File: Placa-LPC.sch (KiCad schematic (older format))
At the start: 23 parts, among them K1 CONN_3, K2 CONN_3, K3 CONN_3, K4 CONN_3, P10 CONN_6, P11 CONN_6, P6 CONN_4X2, P7 CONN_8, P8 CONN_6, P9 CONN_6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

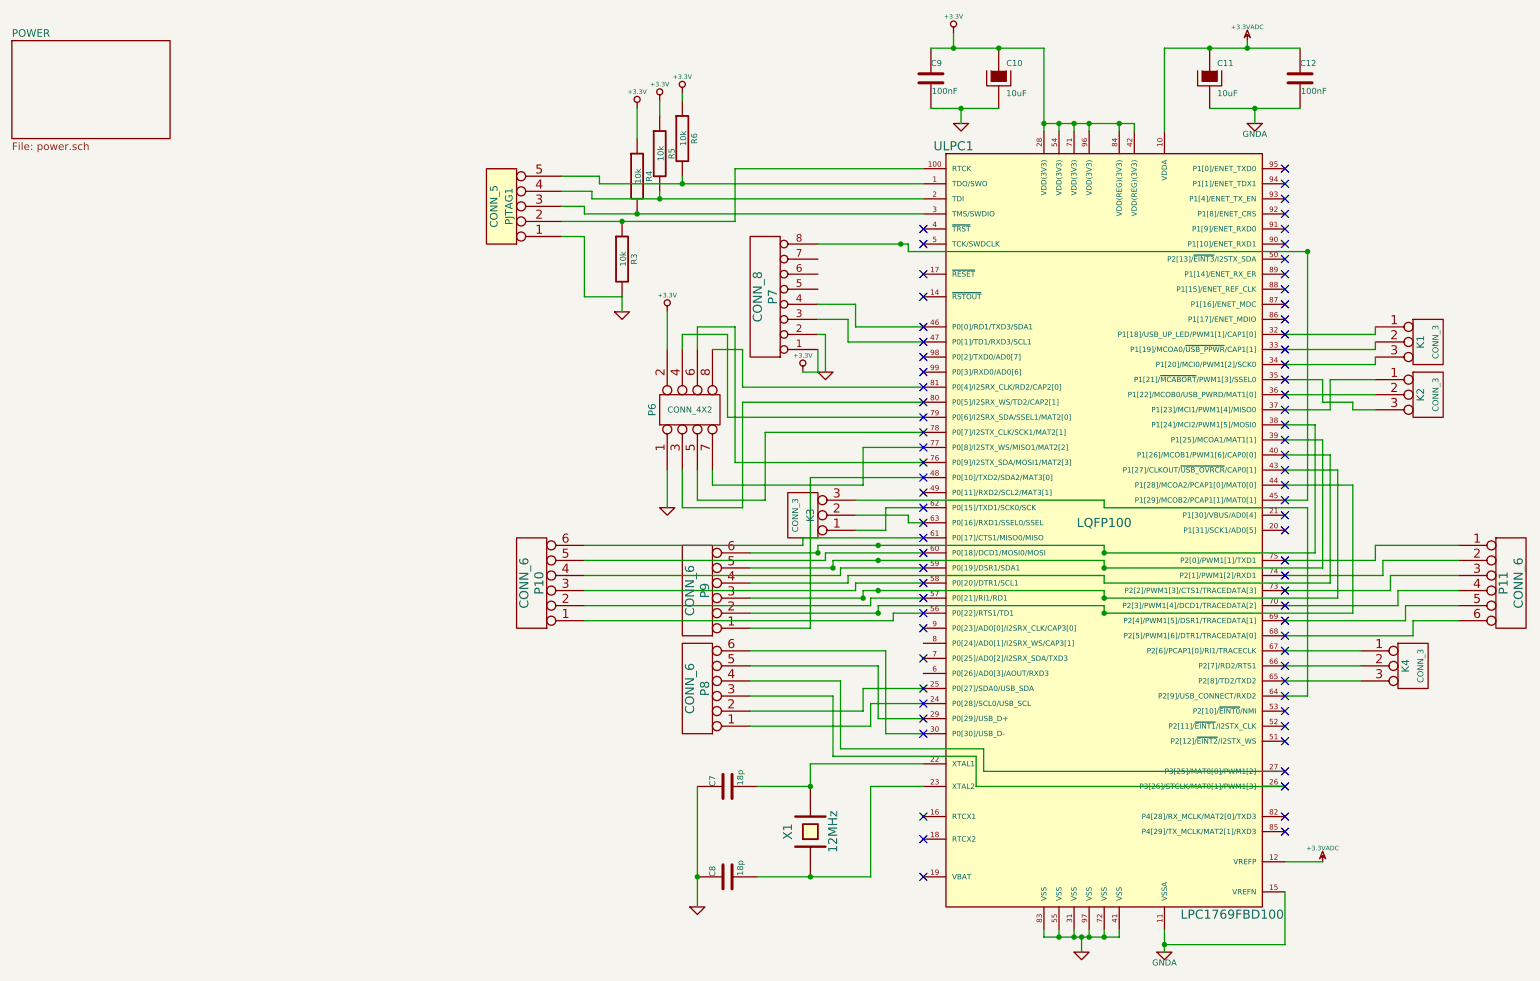
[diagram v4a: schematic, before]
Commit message: Agregado de...
Pines programacion jtag e isp
Resistencias pull-up puerto cero de entrada.
ADC para bateria y reset
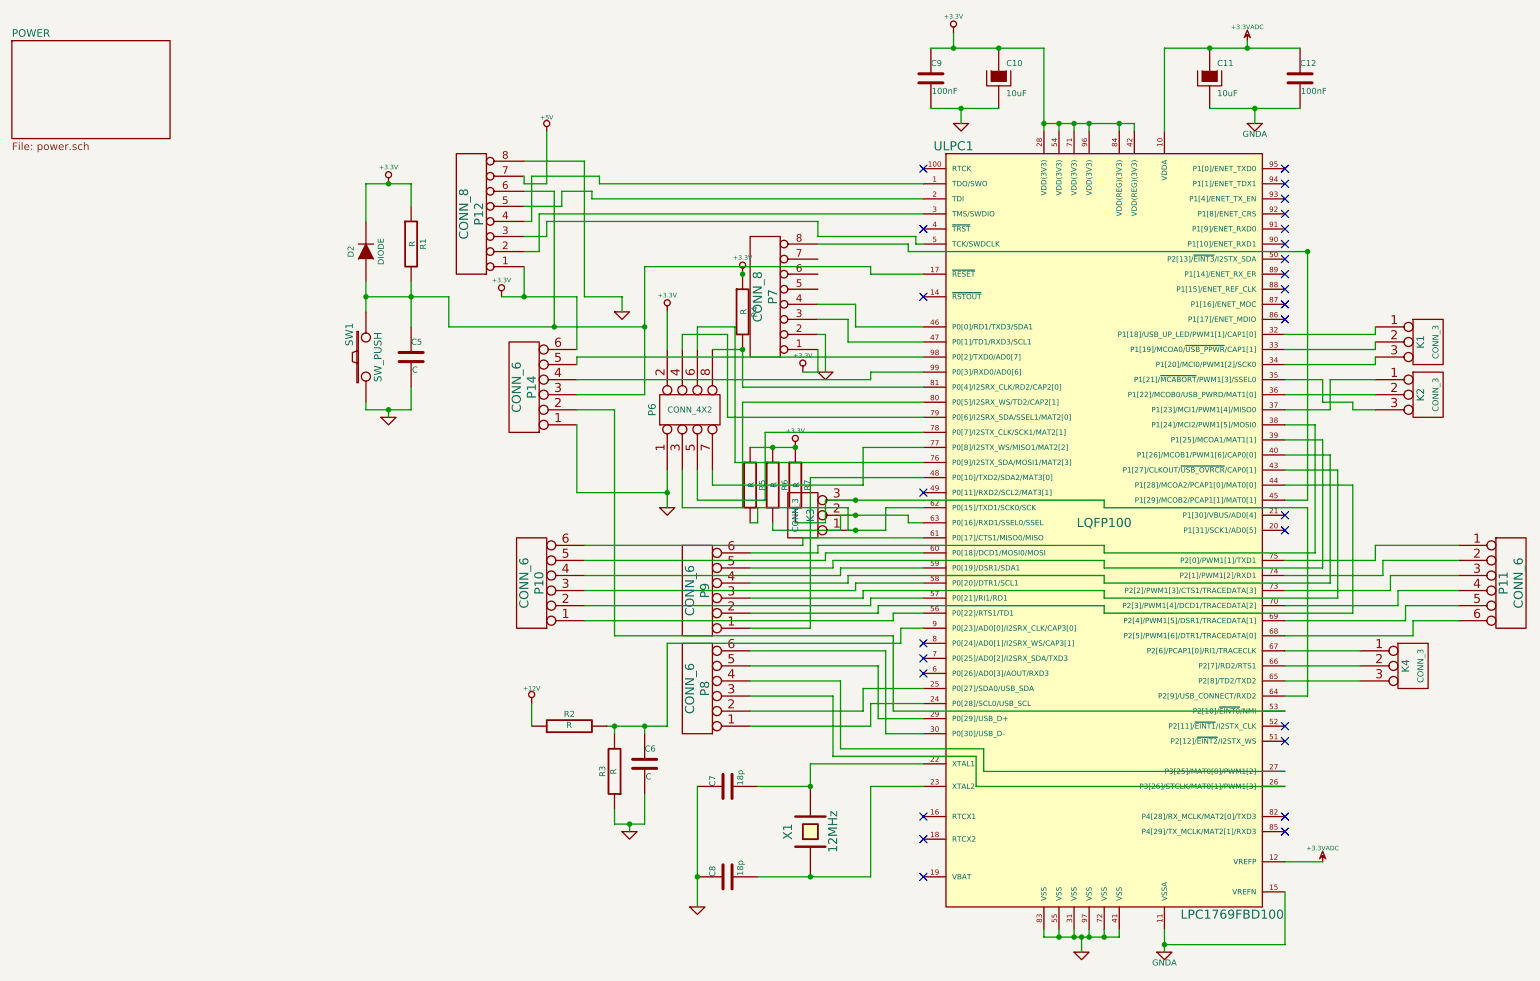
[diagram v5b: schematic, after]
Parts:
- removed PJTAG1: CONN_5, symbol CONN_5
- added C5, C6: C, ~, symbol C
- added D2: DIODE, ~, symbol DIODE
- added P12: CONN_8, symbol CONN_8
- added P14: CONN_6, symbol CONN_6
- added R1, R2, R7: R, ~, symbol R
- added SW1: SW_PUSH, ~, symbol SW_PUSH
- R3, R4, R5, R6: value 10k -> R
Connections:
- net +3.3V: now also D2.2 (K), P12.1 (P1), P14.6, R1.1, R7.1
- net GND: now also R3.1, C5.2, C6.2, P12.8 (P8), P14.1, SW1.1; no longer R3.2
- net at ULPC1.1 (TDO/SWO): now also P12.4 (P4); no longer R6.2
- net at ULPC1.100 (RTCK): no longer R3.1
- net at ULPC1.17 (~RESET~): now also C5.1, D2.1 (A), P12.6 (P6), P14.3, R1.2, SW1.2
- net at ULPC1.2 (TDI): now also P12.5 (P5); no longer R5.2
- net at ULPC1.3 (TMS/SWDIO): now also P12.2 (P2); no longer R4.2
- net at ULPC1.5 (TCK/SWDCLK): now also P12.3 (P3)
- net at ULPC1.53 (P2[10]/~EINT0~/NMI): now also P14.2
- net at K3.1 (P1), ULPC1.62 (P0[15]/TXD1/SCK0/SCK): now also R5.2
- net at K3.2 (PM), ULPC1.63 (P0[16]/RXD1/SSEL0/SSEL): now also R6.2
- net at K3.3 (P3), ULPC1.64 (P2[9]/USB_CONNECT/RXD2): now also R7.2
- net at P6.8, ULPC1.81 (P0[4]/I2SRX_CLK/RD2/CAP2[0]): now also R4.2
- net at ULPC1.9 (P0[23]/AD0[0]/I2SRX_CLK/CAP3[0]): now also R3.2, C6.1, R2.2
- net at ULPC1.98 (P0[2]/TXD0/AD0[7]): now also P14.5
- net at ULPC1.99 (P0[3]/RXD0/AD0[6]): now also P14.4
- new net +12V: R2.1
- new net +5V: P12.7 (P7)
- no-connect marks 75 -> 27

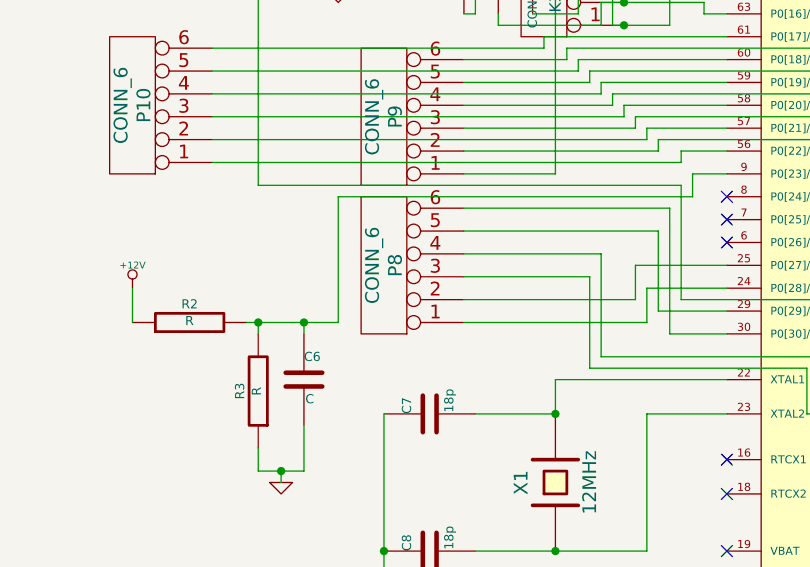
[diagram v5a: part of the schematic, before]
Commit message: Version final
Agregado de resistencias pull up y cambio de pootprint lpc
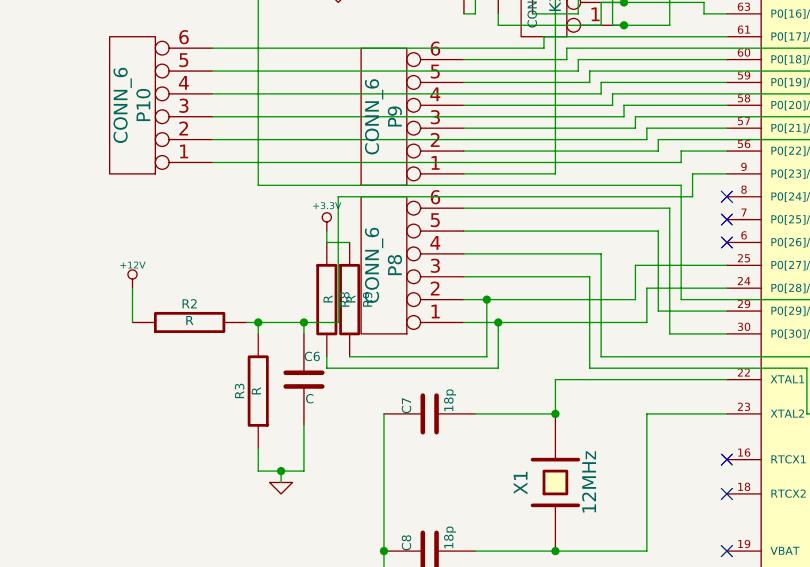
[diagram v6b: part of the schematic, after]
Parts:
- added R8, R9: R, ~, symbol R
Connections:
- net +3.3V: now also R8.1, R9.1
- net at P8.1, ULPC1.24 (P0[28]/SCL0/USB_SCL): now also R8.2
- net at P8.2, ULPC1.25 (P0[27]/SDA0/USB_SDA): now also R9.2
